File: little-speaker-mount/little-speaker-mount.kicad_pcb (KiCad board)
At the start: 2 copper layers, 35 x 121 mm, 4 parts

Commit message: Adjusting dimensions.
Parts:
- added REF**: MountingHole_5mm_Pad_TopBottom, MountingHole:MountingHole_5mm_Pad_TopBottom, F.Cu at (267.0, 203.0)
- added REF**: MountingHole_5mm_Pad_TopBottom, MountingHole:MountingHole_5mm_Pad_TopBottom, F.Cu at (162.5, 57.0)
- added REF**: MountingHole_5mm_Pad_TopBottom, MountingHole:MountingHole_5mm_Pad_TopBottom, F.Cu at (57.0, 130.0)
- added REF**: MountingHole_5mm_Pad_TopBottom, MountingHole:MountingHole_5mm_Pad_TopBottom, F.Cu at (57.0, 203.0)
- added REF**: MountingHole_5mm_Pad_TopBottom, MountingHole:MountingHole_5mm_Pad_TopBottom, F.Cu at (267.0, 130.0)
- added REF**: MountingHole_5mm_Pad_TopBottom, MountingHole:MountingHole_5mm_Pad_TopBottom, F.Cu at (112.5, 57.0)
- added REF**: MountingHole_5mm_Pad_TopBottom, MountingHole:MountingHole_5mm_Pad_TopBottom, F.Cu at (267.0, 57.0)
- added REF**: MountingHole_5mm_Pad_TopBottom, MountingHole:MountingHole_5mm_Pad_TopBottom, F.Cu at (112.5, 203.0)
- added REF**: MountingHole_5mm_Pad_TopBottom, MountingHole:MountingHole_5mm_Pad_TopBottom, F.Cu at (212.5, 203.0)
- added REF**: MountingHole_5mm_Pad_TopBottom, MountingHole:MountingHole_5mm_Pad_TopBottom, F.Cu at (57.0, 57.0)
- added REF**: MountingHole_5mm_Pad_TopBottom, MountingHole:MountingHole_5mm_Pad_TopBottom, F.Cu at (212.5, 57.0)
- added REF**: MountingHole_5mm_Pad_TopBottom, MountingHole:MountingHole_5mm_Pad_TopBottom, F.Cu at (162.5, 203.0)
- moved REF** 57.6 mm to (237.5, 130.0)
- moved REF** 55.5 mm to (187.5, 130.0)
- moved REF** 53.5 mm to (137.5, 130.0)
- moved REF** 51.5 mm to (87.5, 130.0)
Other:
- board size 35 x 121 mm -> 225 x 160 mm

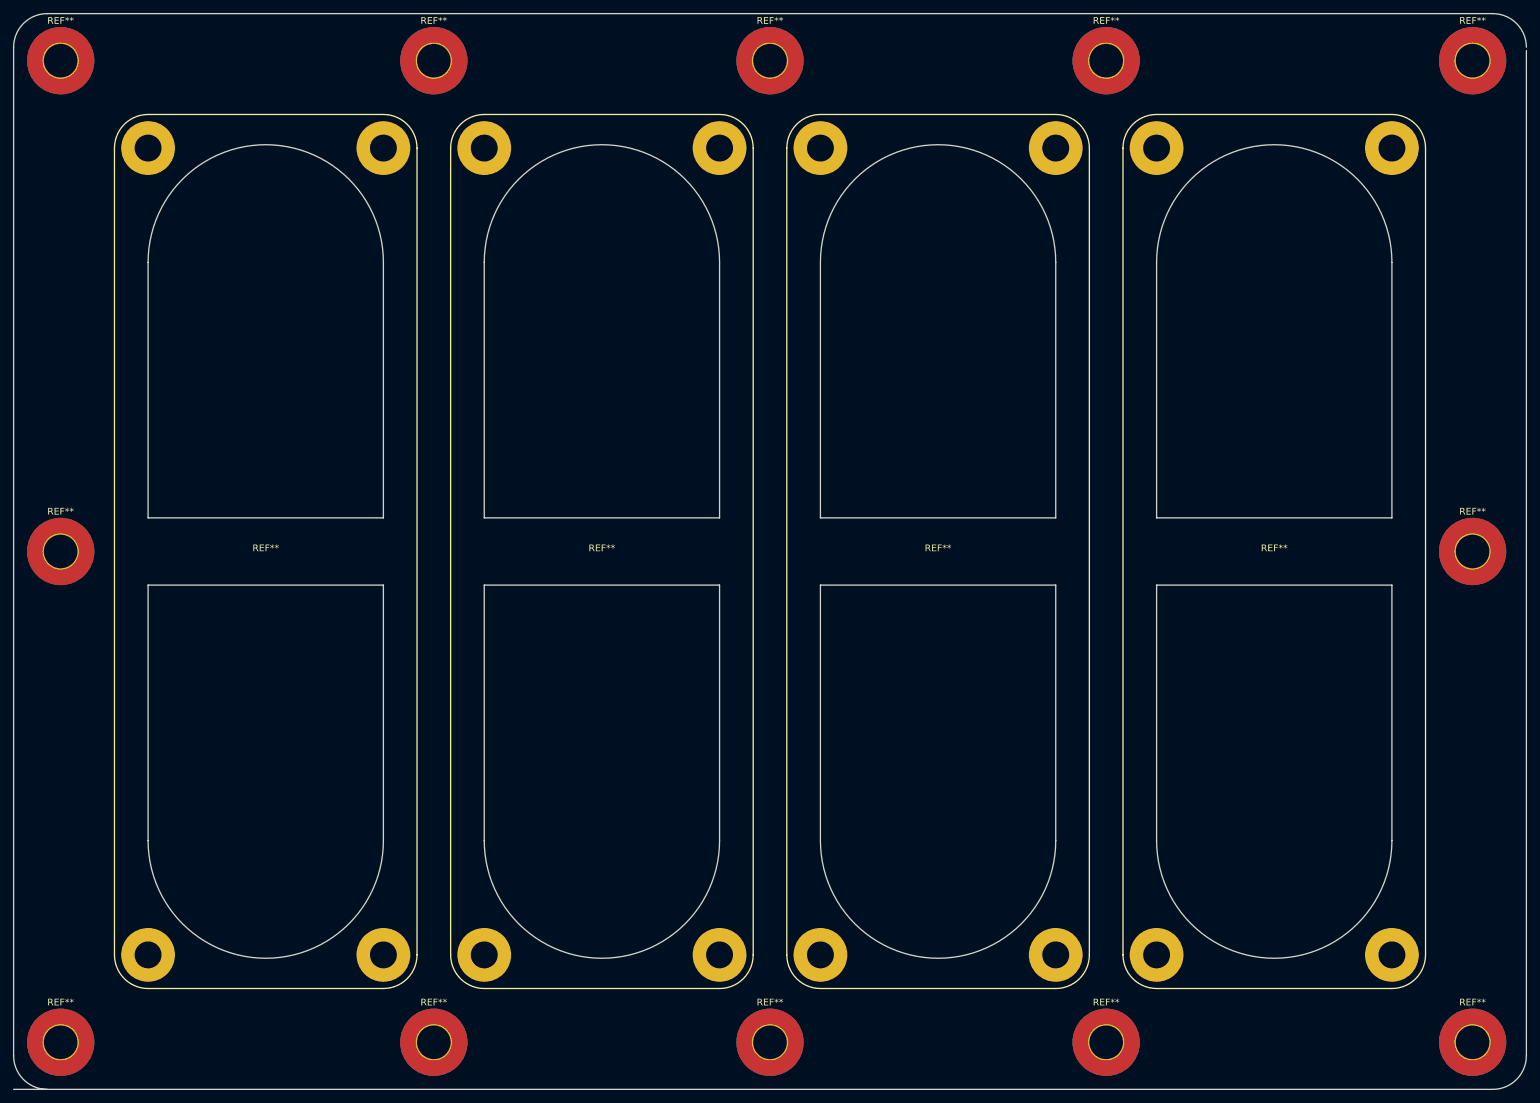
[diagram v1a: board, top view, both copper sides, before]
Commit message: Finished the little speaker mount.
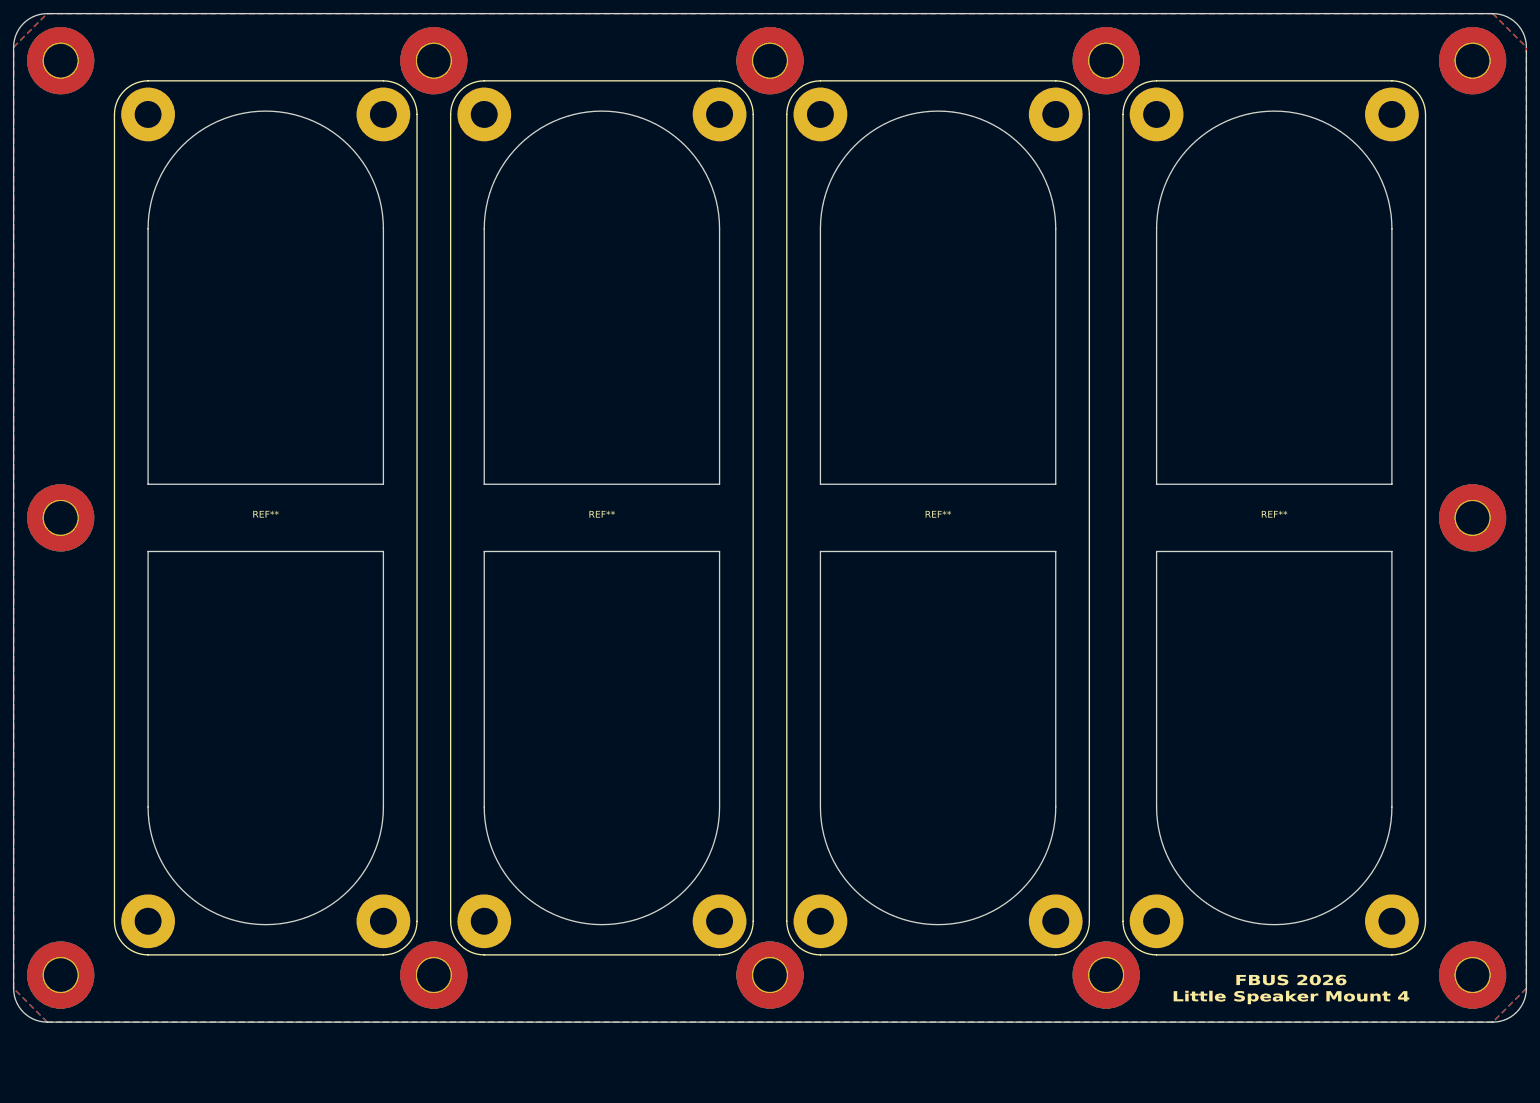
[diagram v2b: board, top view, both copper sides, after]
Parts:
- moved REF** 10.0 mm to (267.0, 193.0)
- moved REF** 10.0 mm to (57.0, 193.0)
- moved REF** 10.0 mm to (112.5, 193.0)
- moved REF** 10.0 mm to (212.5, 193.0)
- moved REF** 10.0 mm to (162.5, 193.0)
- moved REF** 5.00 mm to (187.5, 125.0)
- moved REF** 5.00 mm to (57.0, 125.0)
- moved REF** 5.00 mm to (237.5, 125.0)
- moved REF** 5.00 mm to (267.0, 125.0)
- moved REF** 5.00 mm to (137.5, 125.0)
- moved REF** 5.00 mm to (87.5, 125.0)
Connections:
- REF** pad 1: (no net) -> GND (x12)
- REF** pad : (no net) -> GND (x4)
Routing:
- added copper zone on B.Cu, net GND
- added copper zone on F.Cu, net GND
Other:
- board size 225 x 160 mm -> 225 x 150 mm
- board text added: "FBUS 2026 Little Speaker Mount 4"
